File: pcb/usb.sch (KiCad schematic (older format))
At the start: 9 parts, among them J600 USB_B_Micro, U600 USBLC6-2SC6

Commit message: pcb: working on sch
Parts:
- added U?: MCIMX7S5EVM08SC, footprints:BGA-541_25x25_19.0x19.0mm, symbol symbols:MCIMX7S5EVM08SC
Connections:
- net VBUS: now also U?.C8 (USB_OTG1_VBUS)
- net USB_DM: no longer names the net of R602.1
- net USB_DM: now also U?.A8 (USB_OTG1_DN)
- net USB_DP: no longer names the net of R601.1
- net USB_DP: now also U?.B8 (USB_OTG1_DP)
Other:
- moved on the sheet: C600, C601, D600, D601, J600, R600, R601, R602, U600

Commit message: pcb: working on sch
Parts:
- added C601, C602, C604, C605: 220nF, symbol Device:C
- added C603, C606: 2.2uF, symbol Device:C
- added J?: USB_A, symbol Connector:USB_A
- added R603, R604: 200/1%, Resistor_SMD:R_0805_2012Metric, symbol Device:R
- added R605: 47K, Resistor_SMD:R_0805_2012Metric, symbol Device:R
- added R606, R607: 22, Resistor_SMD:R_0805_2012Metric, symbol Device:R
- gave numbers to parts that had none: 1
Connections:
- net GND: now also C601.2, C602.2, C603.2, C604.2, C605.2, C606.2, J?.4 (GND), J?.5 (Shield), R603.2, R604.2
- net VBUS: now also U100.C10 (USB2_VBUS), J?.1 (VBUS)
- net at D600.1 (A1), J600.4 (ID): now also U100.B7 (USB_OTG1_ID)
- net at U100.A10 (USB_OTG2_DN): now also R607.1
- net at U100.A11 (USB_OTG2_REXT): now also R604.1
- net at U100.A7 (USB1_OTG1_REXT): now also R603.1
- net at U100.B10 (USB_OTG2_DP): now also R606.1
- net at U100.C7 (~USB_OTG1_CHD): now also R605.1
- net +3V3: now reaches U100.F10 (VDD_USB_OTG1_3P3_IN)
- net +3V3: now also U100.F9 (VDD_USB_OTG2_3P3_IN), C601.1, C604.1, R605.2
- net at U100.H10 (VDD_USB_OTG1_1P0_CAP): now also C602.1, C603.1
- net at U100.J11 (VDD_USB_OTG2_1P0_CAP): now also C605.1, C606.1
- new net: J?.2 (D-), R607.2
- new net: J?.3 (D+), R606.2
- no-connect marks 1 -> 4
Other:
- note added: "The Type A port is not ESD protected, and only powered if Type B Micro is connected (shared power). \nThis port is meant for development purpose only."
- moved on the sheet: C600, C601, D600, D601, J600, R600, R601, R602, U100I, U600

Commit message: pcb: finishing sch for r0.1
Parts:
- added R608: 1R, Resistor_SMD:R_0805_2012Metric, symbol Device:R
- C601, C602, C603, C604, C605, C606: footprint (none) -> Capacitor_SMD:C_0402_1005Metric
- J601: renamed from J?; footprint (none) -> Connector_USB:USB_A_Stewart_SS-52100-001_Horizontal
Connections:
- net GND: now also R608.2; no longer C600.2
- new net: C600.2, R608.1
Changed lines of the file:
@@
 $EndComp
 $Comp
-L power:GND #PWR?
+L power:GND #PWR0291
 U 1 1 5C9961F9
 P 7900 2500
-F 0 "#PWR?" H 7900 2250 50  0001 C CNN
+F 0 "#PWR0291" H 7900 2250 50  0001 C CNN
 F 1 "GND" H 7905 2327 50  0000 C CNN
 F 2 "" H 7900 2500 50  0001 C CNN
@@
 $EndComp
 $Comp
-L power:GND #PWR?
+L power:GND #PWR0292
 U 1 1 5C996234
 P 9100 4100
-F 0 "#PWR?" H 9100 3850 50  0001 C CNN
+F 0 "#PWR0292" H 9100 3850 50  0001 C CNN
 F 1 "GND" H 9105 3927 50  0000 C CNN
 F 2 "" H 9100 4100 50  0001 C CNN
@@
 $EndComp
 $Comp
-L power:GND #PWR?
+L power:GND #PWR0293
 U 1 1 5C996258
 P 8100 3900
-F 0 "#PWR?" H 8100 3650 50  0001 C CNN
+F 0 "#PWR0293" H 8100 3650 50  0001 C CNN
 F 1 "GND" H 8105 3727 50  0000 C CNN
 F 2 "" H 8100 3900 50  0001 C CNN
@@
 $EndComp
 $Comp
-L power:GND #PWR?
+L power:GND #PWR0294
 U 1 1 5C99627A
-P 5900 2400
-F 0 "#PWR?" H 5900 2150 50  0001 C CNN
-F 1 "GND" H 5905 2227 50  0000 C CNN
-F 2 "" H 5900 2400 50  0001 C CNN
-F 3 "" H 5900 2400 50  0001 C CNN
-	1    5900 2400
-	-1   0    0    -1
-$EndComp
-$Comp
-L power:VBUS #PWR?
+P 5900 2600
+F 0 "#PWR0294" H 5900 2350 50  0001 C CNN
+F 1 "GND" H 5905 2427 50  0000 C CNN
+F 2 "" H 5900 2600 50  0001 C CNN
+F 3 "" H 5900 2600 50  0001 C CNN
+	1    5900 2600
+	-1   0    0    -1
+$EndComp
+$Comp
+L power:VBUS #PWR0295
 U 1 1 5C9962B3
 P 5900 1900
-F 0 "#PWR?" H 5900 1750 50  0001 C CNN
+F 0 "#PWR0295" H 5900 1750 50  0001 C CNN
 F 1 "VBUS" H 5915 2073 50  0000 C CNN
 F 2 "" H 5900 1900 50  0001 C CNN
@@
 Wire Wire Line
 	8700 3100 8500 3100
-Wire Wire Line
-	5900 2300 5900 2400
 Wire Wire Line
 	8100 3400 8100 3200
@@
 $EndComp
 $Comp
-L power:GND #PWR?
+L power:GND #PWR0296
 U 1 1 5D1E2A0C
 P 6100 3700
-F 0 "#PWR?" H 6100 3450 50  0001 C CNN
+F 0 "#PWR0296" H 6100 3450 50  0001 C CNN
 F 1 "GND" H 6105 3527 50  0000 C CNN
 F 2 "" H 6100 3700 50  0001 C CNN
@@
 $EndComp
 $Comp
-L power:GND #PWR?
+L power:GND #PWR0297
 U 1 1 5D1E42CE
 P 5900 4500
-F 0 "#PWR?" H 5900 4250 50  0001 C CNN
+F 0 "#PWR0297" H 5900 4250 50  0001 C CNN
 F 1 "GND" H 5905 4327 50  0000 C CNN
 F 2 "" H 5900 4500 50  0001 C CNN
@@
 $EndComp
 $Comp
-L power:+3V3 #PWR?
+L power:+3V3 #PWR0298
 U 1 1 5D1E9321
 P 6100 3600
-F 0 "#PWR?" H 6100 3450 50  0001 C CNN
+F 0 "#PWR0298" H 6100 3450 50  0001 C CNN
 F 1 "+3V3" H 6100 3750 50  0000 C CNN
 F 2 "" H 6100 3600 50  0001 C CNN
@@
 NoConn ~ 5300 4800
 $Comp
-L power:+3V3 #PWR?
+L power:+3V3 #PWR0299
 U 1 1 5D20C9B4
 P 2500 3200
-F 0 "#PWR?" H 2500 3050 50  0001 C CNN
+F 0 "#PWR0299" H 2500 3050 50  0001 C CNN
 F 1 "+3V3" H 2500 3350 50  0000 C CNN
 F 2 "" H 2500 3200 50  0001 C CNN
@@
 F 0 "C602" H 3015 3696 50  0000 L CNN
 F 1 "220nF" H 3015 3605 50  0000 L CNN
-F 2 "" H 2938 3500 50  0001 C CNN
+F 2 "Capacitor_SMD:C_0402_1005Metric" H 2938 3500 50  0001 C CNN
 F 3 "~" H 2900 3650 50  0001 C CNN
 	1    2900 3650
@@
 F 0 "C603" H 3415 3696 50  0000 L CNN
 F 1 "2.2uF" H 3415 3605 50  0000 L CNN
-F 2 "" H 3338 3500 50  0001 C CNN
+F 2 "Capacitor_SMD:C_0402_1005Metric" H 3338 3500 50  0001 C CNN
 F 3 "~" H 3300 3650 50  0001 C CNN
 	1    3300 3650
@@
 P 2900 3800
 AR Path="/5D5090CA/5D2271E4" Ref="#PWR?"  Part="1"
-AR Path="/5D1A413B/5D2271E4" Ref="#PWR?"  Part="1"
-F 0 "#PWR?" H 2900 3550 50  0001 C CNN
+AR Path="/5D1A413B/5D2271E4" Ref="#PWR0300"  Part="1"
+F 0 "#PWR0300" H 2900 3550 50  0001 C CNN
 F 1 "GND" H 2905 3627 50  0000 C CNN
 F 2 "" H 2900 3800 50  0001 C CNN
@@
 F 0 "C601" H 2615 3396 50  0000 L CNN
 F 1 "220nF" H 2615 3305 50  0000 L CNN
-F 2 "" H 2538 3200 50  0001 C CNN
+F 2 "Capacitor_SMD:C_0402_1005Metric" H 2538 3200 50  0001 C CNN
 F 3 "~" H 2500 3350 50  0001 C CNN
 	1    2500 3350
@@
 P 2500 3500
 AR Path="/5D5090CA/5D22AF19" Ref="#PWR?"  Part="1"
-AR Path="/5D1A413B/5D22AF19" Ref="#PWR?"  Part="1"
-F 0 "#PWR?" H 2500 3250 50  0001 C CNN
+AR Path="/5D1A413B/5D22AF19" Ref="#PWR0301"  Part="1"
+F 0 "#PWR0301" H 2500 3250 50  0001 C CNN
 F 1 "GND" H 2505 3327 50  0000 C CNN
 F 2 "" H 2500 3500 50  0001 C CNN
@@
 Connection ~ 2500 3200
 $Comp
-L power:+3V3 #PWR?
+L power:+3V3 #PWR0302
 U 1 1 5D22EAC8
 P 2500 4100
-F 0 "#PWR?" H 2500 3950 50  0001 C CNN
+F 0 "#PWR0302" H 2500 3950 50  0001 C CNN
 F 1 "+3V3" H 2500 4250 50  0000 C CNN
 F 2 "" H 2500 4100 50  0001 C CNN
@@
 F 0 "C605" H 3015 4596 50  0000 L CNN
 F 1 "220nF" H 3015 4505 50  0000 L CNN
-F 2 "" H 2938 4400 50  0001 C CNN
+F 2 "Capacitor_SMD:C_0402_1005Metric" H 2938 4400 50  0001 C CNN
 F 3 "~" H 2900 4550 50  0001 C CNN
 	1    2900 4550
@@
 F 0 "C606" H 3415 4596 50  0000 L CNN
 F 1 "2.2uF" H 3415 4505 50  0000 L CNN
-F 2 "" H 3338 4400 50  0001 C CNN
+F 2 "Capacitor_SMD:C_0402_1005Metric" H 3338 4400 50  0001 C CNN
 F 3 "~" H 3300 4550 50  0001 C CNN
 	1    3300 4550
@@
 P 2900 4700
 AR Path="/5D5090CA/5D22EADD" Ref="#PWR?"  Part="1"
-AR Path="/5D1A413B/5D22EADD" Ref="#PWR?"  Part="1"
-F 0 "#PWR?" H 2900 4450 50  0001 C CNN
+AR Path="/5D1A413B/5D22EADD" Ref="#PWR0303"  Part="1"
+F 0 "#PWR0303" H 2900 4450 50  0001 C CNN
 F 1 "GND" H 2905 4527 50  0000 C CNN
 F 2 "" H 2900 4700 50  0001 C CNN
@@
 F 0 "C604" H 2615 4296 50  0000 L CNN
 F 1 "220nF" H 2615 4205 50  0000 L CNN
-F 2 "" H 2538 4100 50  0001 C CNN
+F 2 "Capacitor_SMD:C_0402_1005Metric" H 2538 4100 50  0001 C CNN
 F 3 "~" H 2500 4250 50  0001 C CNN
 	1    2500 4250
@@
 P 2500 4400
 AR Path="/5D5090CA/5D22EAEB" Ref="#PWR?"  Part="1"
-AR Path="/5D1A413B/5D22EAEB" Ref="#PWR?"  Part="1"
-F 0 "#PWR?" H 2500 4150 50  0001 C CNN
+AR Path="/5D1A413B/5D22EAEB" Ref="#PWR0304"  Part="1"
+F 0 "#PWR0304" H 2500 4150 50  0001 C CNN
 F 1 "GND" H 2505 4227 50  0000 C CNN
 F 2 "" H 2500 4400 50  0001 C CNN
@@
 Connection ~ 8100 3200
 $Comp
-L Connector:USB_A J?
+L Connector:USB_A J601
 U 1 1 5D26CBC2
 P 9000 4800
-F 0 "J?" H 8770 4789 50  0000 R CNN
+F 0 "J601" H 8770 4789 50  0000 R CNN
 F 1 "USB_A" H 8770 4698 50  0000 R CNN
-F 2 "" H 9150 4750 50  0001 C CNN
+F 2 "Connector_USB:USB_A_Stewart_SS-52100-001_Horizontal" H 9150 4750 50  0001 C CNN
 F 3 " ~" H 9150 4750 50  0001 C CNN
 	1    9000 4800
@@
 NoConn ~ 5300 4200
 $Comp
-L power:GND #PWR?
+L power:GND #PWR0305
 U 1 1 5D29CE39
 P 9100 5300
-F 0 "#PWR?" H 9100 5050 50  0001 C CNN
+F 0 "#PWR0305" H 9100 5050 50  0001 C CNN
 F 1 "GND" H 9105 5127 50  0000 C CNN
 F 2 "" H 9100 5300 50  0001 C CNN
@@
 Text Notes 7000 5800 0    50   ~ 0
 The Type A port is not ESD protected, and only powered if Type B Micro is connected (shared power). \nThis port is meant for development purpose only.
+$Comp
+L Device:R R608
+U 1 1 5D2D5A0B
+P 5900 2450
+F 0 "R608" H 5970 2496 50  0000 L CNN
+F 1 "1R" H 5970 2405 50  0000 L CNN
+F 2 "Resistor_SMD:R_0805_2012Metric" V 5830 2450 50  0001 C CNN
+F 3 "~" H 5900 2450 50  0001 C CNN
+	1    5900 2450
+	-1   0    0    -1
+$EndComp
 $EndSCHEMATC

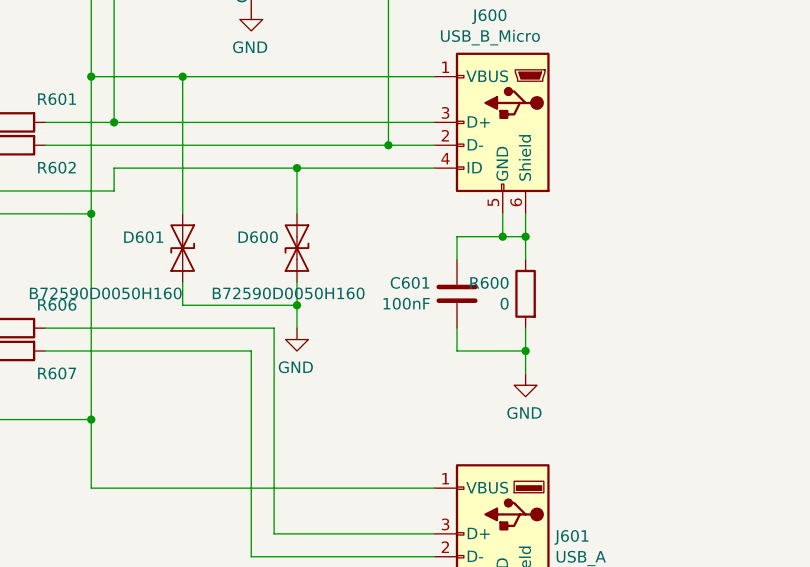
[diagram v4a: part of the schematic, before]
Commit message: pcb: initial netlist
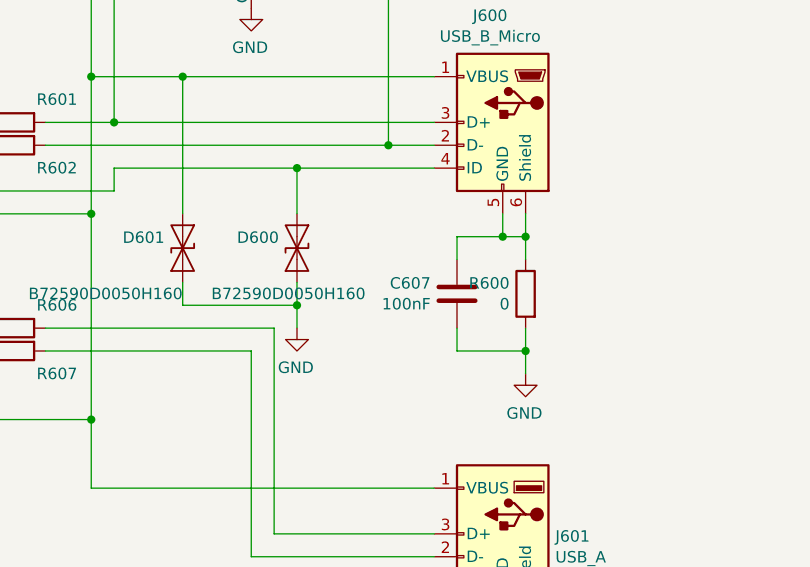
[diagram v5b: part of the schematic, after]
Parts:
- renumbered C601 to C607
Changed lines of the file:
@@
 $EndComp
 $Comp
-L Device:C C601
+L Device:C C607
 U 1 1 5C995EF6
 P 8800 3750
-F 0 "C601" H 8915 3796 50  0000 L CNN
+F 0 "C607" H 8915 3796 50  0000 L CNN
 F 1 "100nF" H 8915 3705 50  0000 L CNN
 F 2 "Capacitor_SMD:C_0805_2012Metric" H 8838 3600 50  0001 C CNN

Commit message: pcb: working on layout
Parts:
- C600: footprint Capacitor_SMD:C_0805_2012Metric -> Capacitor_SMD:C_0603_1608Metric
- R601, R602, R603, R604, R605, R606, R607, R608: footprint Resistor_SMD:R_0805_2012Metric -> Resistor_SMD:R_0603_1608Metric
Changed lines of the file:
@@
 F 0 "R601" V 6750 2800 50  0000 C CNN
 F 1 "22" V 6750 3200 50  0000 C CNN
-F 2 "Resistor_SMD:R_0805_2012Metric" V 6780 3000 50  0001 C CNN
+F 2 "Resistor_SMD:R_0603_1608Metric" V 6780 3000 50  0001 C CNN
 F 3 "~" H 6850 3000 50  0001 C CNN
 	1    6850 3000
@@
 F 0 "R602" V 6950 2900 50  0000 C CNN
 F 1 "22" V 6950 3300 50  0000 C CNN
-F 2 "Resistor_SMD:R_0805_2012Metric" V 6780 3100 50  0001 C CNN
+F 2 "Resistor_SMD:R_0603_1608Metric" V 6780 3100 50  0001 C CNN
 F 3 "~" H 6850 3100 50  0001 C CNN
 	1    6850 3100
@@
 F 0 "C600" H 6015 2196 50  0000 L CNN
 F 1 "10uF" H 6015 2105 50  0000 L CNN
-F 2 "Capacitor_SMD:C_0805_2012Metric" H 5938 2000 50  0001 C CNN
+F 2 "Capacitor_SMD:C_0603_1608Metric" H 5938 2000 50  0001 C CNN
 F 3 "~" H 5900 2150 50  0001 C CNN
 	1    5900 2150
@@
 F 0 "R603" V 5600 3950 50  0000 C CNN
 F 1 "200/1%" V 5600 3400 50  0000 C CNN
-F 2 "Resistor_SMD:R_0805_2012Metric" V 5580 3700 50  0001 C CNN
+F 2 "Resistor_SMD:R_0603_1608Metric" V 5580 3700 50  0001 C CNN
 F 3 "~" H 5650 3700 50  0001 C CNN
 	1    5650 3700
@@
 F 0 "R604" V 5600 4750 50  0000 C CNN
 F 1 "200/1%" V 5600 4200 50  0000 C CNN
-F 2 "Resistor_SMD:R_0805_2012Metric" V 5580 4500 50  0001 C CNN
+F 2 "Resistor_SMD:R_0603_1608Metric" V 5580 4500 50  0001 C CNN
 F 3 "~" H 5650 4500 50  0001 C CNN
 	1    5650 4500
@@
 F 0 "R605" V 5600 3850 50  0000 C CNN
 F 1 "47K" V 5600 3300 50  0000 C CNN
-F 2 "Resistor_SMD:R_0805_2012Metric" V 5580 3600 50  0001 C CNN
+F 2 "Resistor_SMD:R_0603_1608Metric" V 5580 3600 50  0001 C CNN
 F 3 "~" H 5650 3600 50  0001 C CNN
 	1    5650 3600
@@
 F 0 "R606" V 6750 3700 50  0000 C CNN
 F 1 "22" V 6750 4100 50  0000 C CNN
-F 2 "Resistor_SMD:R_0805_2012Metric" V 6780 3900 50  0001 C CNN
+F 2 "Resistor_SMD:R_0603_1608Metric" V 6780 3900 50  0001 C CNN
 F 3 "~" H 6850 3900 50  0001 C CNN
 	1    6850 3900
@@
 F 0 "R607" V 6950 3800 50  0000 C CNN
 F 1 "22" V 6950 4200 50  0000 C CNN
-F 2 "Resistor_SMD:R_0805_2012Metric" V 6780 4000 50  0001 C CNN
+F 2 "Resistor_SMD:R_0603_1608Metric" V 6780 4000 50  0001 C CNN
 F 3 "~" H 6850 4000 50  0001 C CNN
 	1    6850 4000
@@
 F 0 "R608" H 5970 2496 50  0000 L CNN
 F 1 "1R" H 5970 2405 50  0000 L CNN
-F 2 "Resistor_SMD:R_0805_2012Metric" V 5830 2450 50  0001 C CNN
+F 2 "Resistor_SMD:R_0603_1608Metric" V 5830 2450 50  0001 C CNN
 F 3 "~" H 5900 2450 50  0001 C CNN
 	1    5900 2450

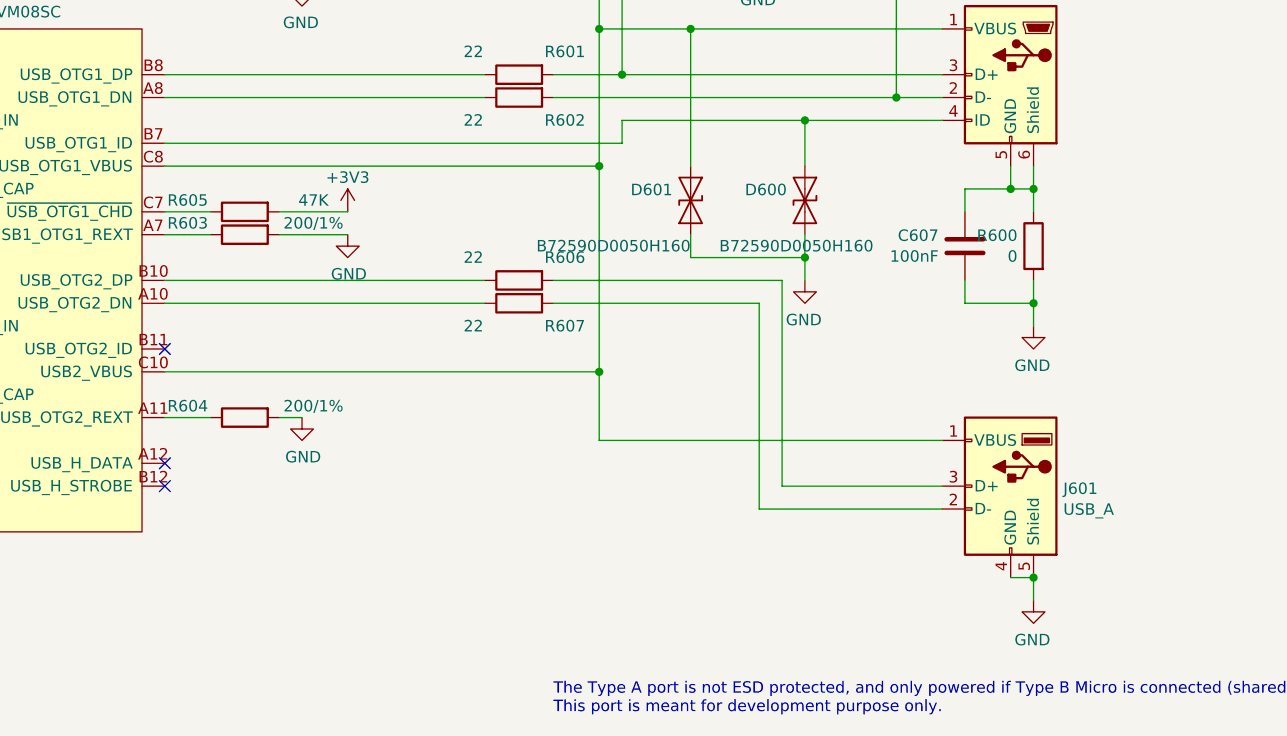
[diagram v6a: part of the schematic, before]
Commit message: pcb: add board outline
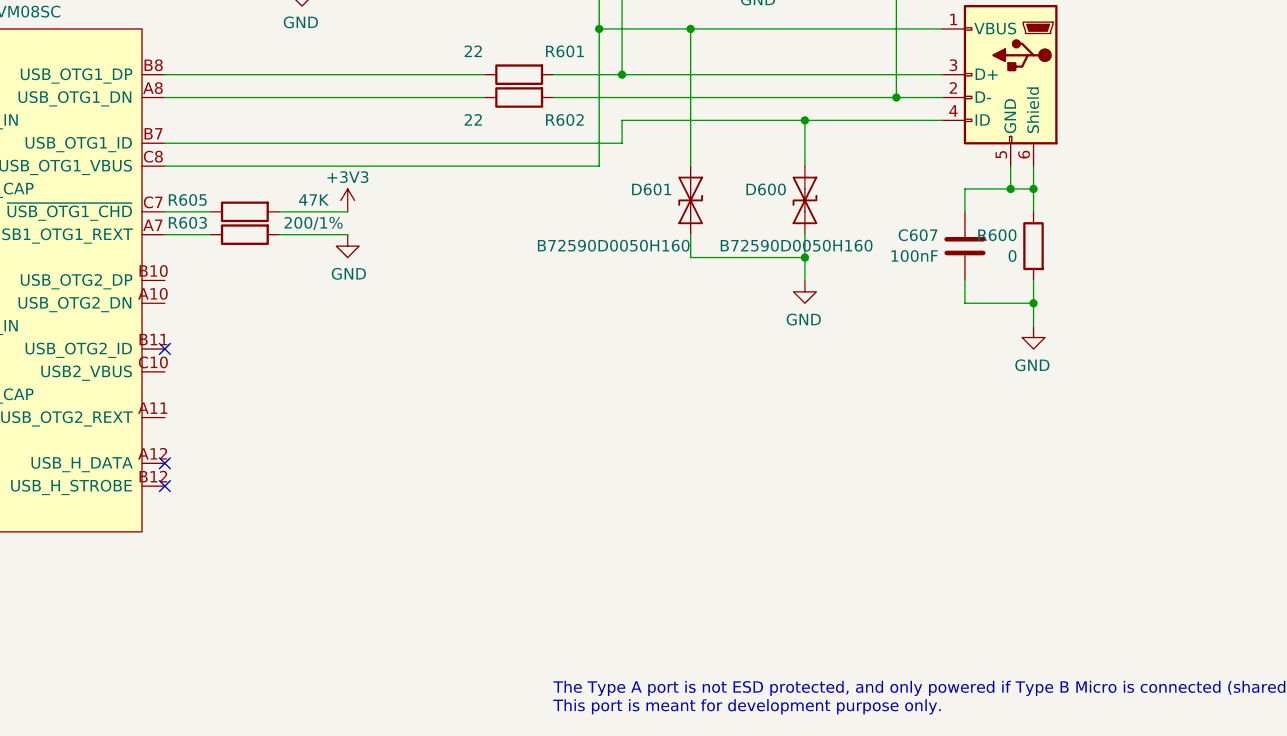
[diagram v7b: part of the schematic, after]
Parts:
- removed J601: USB_A, Connector_USB:USB_A_Stewart_SS-52100-001_Horizontal, symbol Connector:USB_A
- removed R604: 200/1%, Resistor_SMD:R_0603_1608Metric, symbol Device:R
- removed R606, R607: 22, Resistor_SMD:R_0603_1608Metric, symbol Device:R
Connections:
- net VBUS: no longer U100.C10 (USB2_VBUS)
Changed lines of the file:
@@
-$EndComp
-$Comp
-L Device:R R604
-U 1 1 5D1E1E89
-P 5650 4500
-F 0 "R604" V 5600 4750 50  0000 C CNN
-F 1 "200/1%" V 5600 4200 50  0000 C CNN
-F 2 "Resistor_SMD:R_0603_1608Metric" V 5580 4500 50  0001 C CNN
-F 3 "~" H 5650 4500 50  0001 C CNN
-	1    5650 4500
-	0    -1   1    0
 $EndComp
 $Comp
@@
 	1    0    0    -1
 $EndComp
-$Comp
-L power:GND #PWR0297
-U 1 1 5D1E42CE
-P 5900 4500
-F 0 "#PWR0297" H 5900 4250 50  0001 C CNN
-F 1 "GND" H 5905 4327 50  0000 C CNN
-F 2 "" H 5900 4500 50  0001 C CNN
-F 3 "" H 5900 4500 50  0001 C CNN
-	1    5900 4500
-	1    0    0    -1
-$EndComp
-Wire Wire Line
-	5900 4500 5800 4500
-Wire Wire Line
-	5300 4500 5500 4500
 Wire Wire Line
 	5300 3700 5500 3700
@@
 	7300 3200 7300 3300
 Connection ~ 8100 3200
-$Comp
-L Connector:USB_A J601
-U 1 1 5D26CBC2
-P 9000 4800
-F 0 "J601" H 8770 4789 50  0000 R CNN
-F 1 "USB_A" H 8770 4698 50  0000 R CNN
-F 2 "Connector_USB:USB_A_Stewart_SS-52100-001_Horizontal" H 9150 4750 50  0001 C CNN
-F 3 " ~" H 9150 4750 50  0001 C CNN
-	1    9000 4800
-	-1   0    0    -1
-$EndComp
 Wire Wire Line
 	5900 1900 5900 2000
@@
 Wire Wire Line
 	5300 3400 7200 3400
-$Comp
-L Device:R R606
-U 1 1 5D28A3E2
-P 6850 3900
-F 0 "R606" V 6750 3700 50  0000 C CNN
-F 1 "22" V 6750 4100 50  0000 C CNN
-F 2 "Resistor_SMD:R_0603_1608Metric" V 6780 3900 50  0001 C CNN
-F 3 "~" H 6850 3900 50  0001 C CNN
-	1    6850 3900
-	0    -1   1    0
-$EndComp
-$Comp
-L Device:R R607
-U 1 1 5D28A3E8
-P 6850 4000
-F 0 "R607" V 6950 3800 50  0000 C CNN
-F 1 "22" V 6950 4200 50  0000 C CNN
-F 2 "Resistor_SMD:R_0603_1608Metric" V 6780 4000 50  0001 C CNN
-F 3 "~" H 6850 4000 50  0001 C CNN
-	1    6850 4000
-	0    -1   1    0
-$EndComp
-Wire Wire Line
-	7000 3900 8000 3900
-Wire Wire Line
-	8000 3900 8000 4800
-Wire Wire Line
-	8000 4800 8700 4800
-Wire Wire Line
-	8700 4900 7900 4900
-Wire Wire Line
-	7900 4900 7900 4000
-Wire Wire Line
-	7900 4000 7000 4000
-Wire Wire Line
-	6700 3900 5300 3900
-Wire Wire Line
-	5300 4000 6700 4000
-Wire Wire Line
-	5300 4300 7200 4300
-Wire Wire Line
-	7200 4300 7200 3400
-Connection ~ 7200 3400
 Wire Wire Line
 	7600 2800 8700 2800
-Wire Wire Line
-	7200 4600 7200 4300
-Wire Wire Line
-	7200 4600 8700 4600
-Connection ~ 7200 4300
 NoConn ~ 5300 4200
-$Comp
-L power:GND #PWR0305
-U 1 1 5D29CE39
-P 9100 5300
-F 0 "#PWR0305" H 9100 5050 50  0001 C CNN
-F 1 "GND" H 9105 5127 50  0000 C CNN
-F 2 "" H 9100 5300 50  0001 C CNN
-F 3 "" H 9100 5300 50  0001 C CNN
-	1    9100 5300
-	-1   0    0    -1
-$EndComp
-Wire Wire Line
-	9100 5300 9100 5200
-Wire Wire Line
-	9000 5200 9100 5200
-Connection ~ 9100 5200
 Text Notes 7000 5800 0    50   ~ 0
 The Type A port is not ESD protected, and only powered if Type B Micro is connected (shared power). \nThis port is meant for development purpose only.
